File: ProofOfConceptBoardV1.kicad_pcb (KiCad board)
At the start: 2 copper layers, 37 parts, among them U1 MCP2515-EST, U2 MCP2515-EST

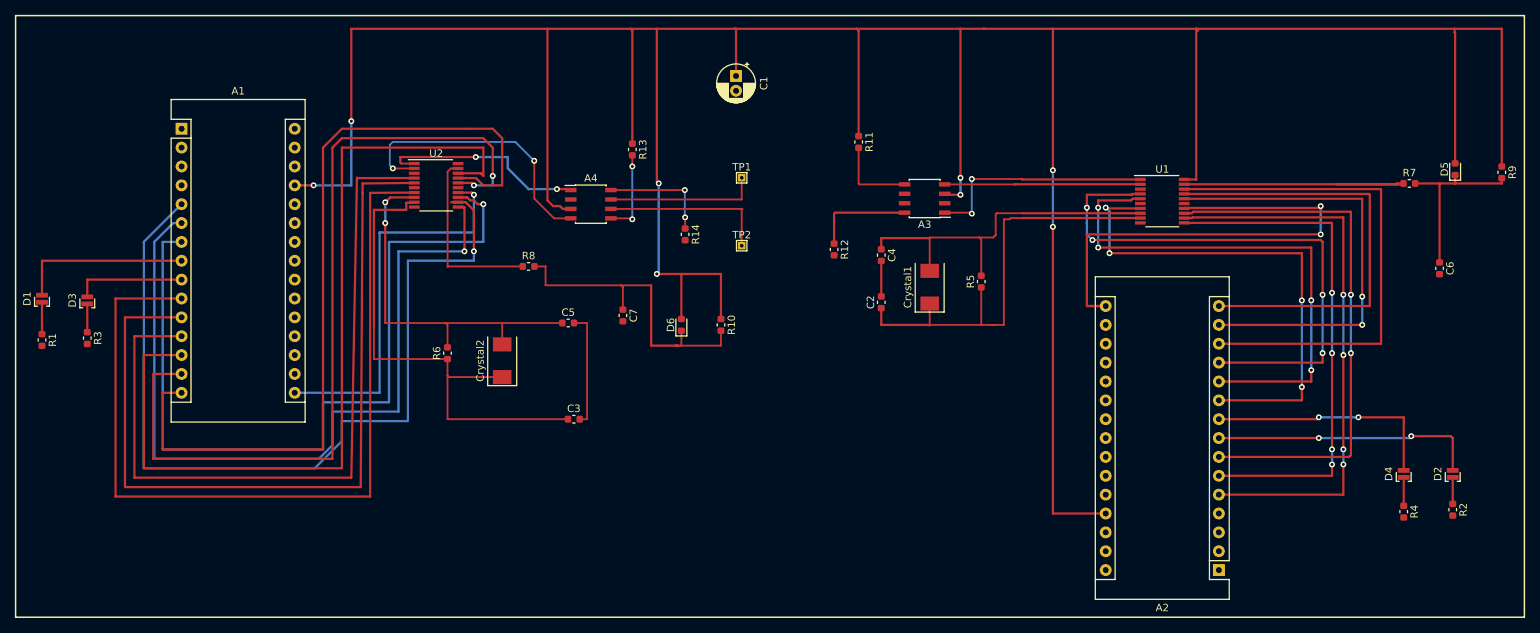
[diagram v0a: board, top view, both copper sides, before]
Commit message: 0.0.4 Fixed some PCB Connections and adjusted Top and Bot Ground Plane
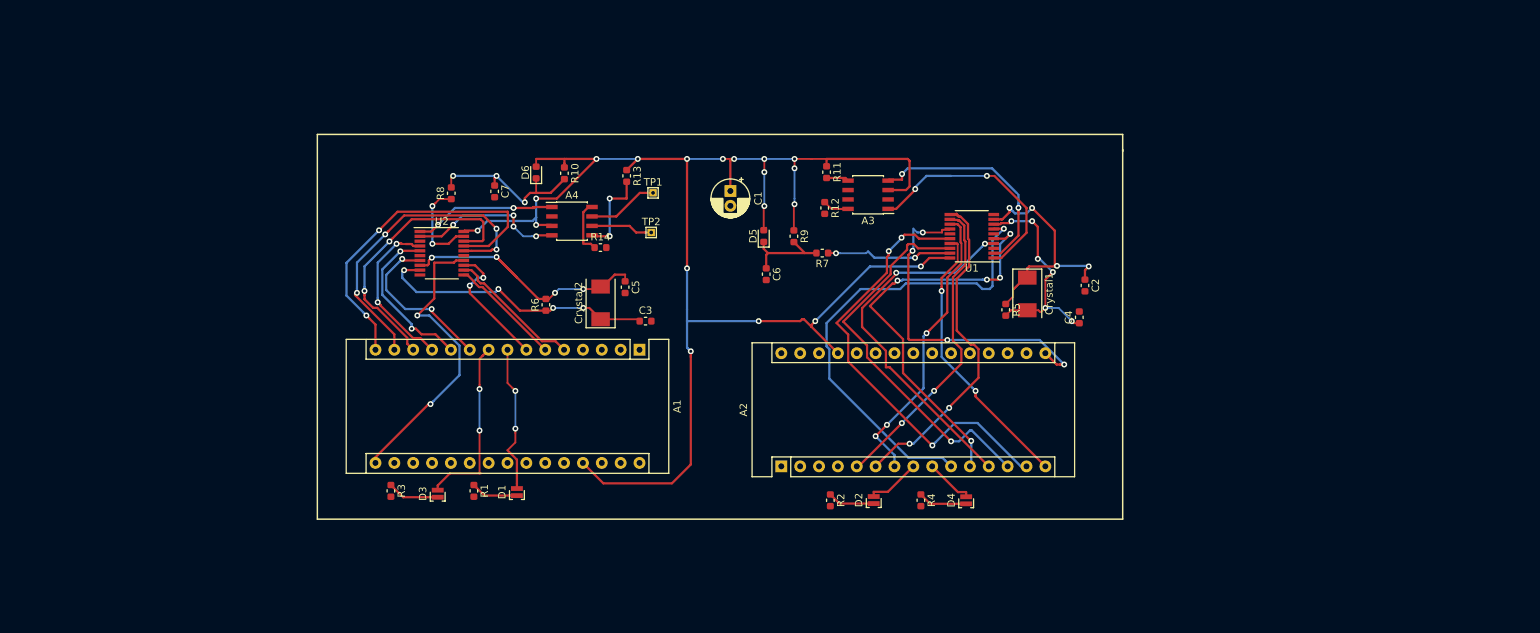
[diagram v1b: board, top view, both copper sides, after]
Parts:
- moved R9 95.7 mm to (133.3, 70.4)
- moved D5 93.6 mm to (129.2, 70.3)
- moved C6 90.7 mm to (129.5, 75.5)
- moved R2 83.8 mm to (138.2, 105.9)
- moved R7 79.6 mm to (137.1, 72.6), turned to 180 degrees
- moved D2 78.1 mm to (144.0, 105.9)
- moved D1 69.1 mm to (96.0, 104.8)
- moved A1 68.5 mm to (112.5, 85.6), turned to 270 degrees
- moved R4 65.0 mm to (150.4, 105.9)
- moved R1 61.6 mm to (90.2, 104.6)
- moved A2 60.6 mm to (131.6, 101.3), turned to 90 degrees
- moved D4 59.0 mm to (156.5, 105.9)
- moved D3 53.9 mm to (85.3, 105.0)
- moved R3 45.8 mm to (79.0, 104.6)
- moved R10 29.4 mm to (102.4, 61.9)
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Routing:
- net +5V: track 457.3 -> 216.8 mm, vias 8 -> 19
- net INT0_2: track 118.2 -> 18.3 mm, vias 1 -> 0
- net TBUF0_2: track 116.7 -> 22.4 mm, vias 0 -> 2
- net INT1_2: track 109.3 -> 15.2 mm, vias 1 -> 0
- net INTMCP_2: track 110.5 -> 17.7 mm, vias 1 -> 2
- net TBUF1_2: track 110.1 -> 22.2 mm, vias 0 -> 2
- net TBUF2_2: track 102.7 -> 22.6 mm, vias 0 -> 2
- net SS_2: track 116.6 -> 38.2 mm, vias 0 -> 2
- net MOSI_2: track 113.8 -> 43.6 mm, vias 2 -> 4
- net MISO_2: track 110.8 -> 46.9 mm, vias 0 -> 2
- net INT0: track 75.6 -> 41.9 mm, vias 4 -> 2
- net INTMCP: track 73.2 -> 39.7 mm, vias 2 -> 3
- net OSC1_2: track 68.1 -> 38.4 mm, vias 0 -> 4
- net Net-(A2-Pad8): track 36.1 -> 7.39 mm, vias 2 -> 0
- net OSC1: track 60.4 -> 34.7 mm, vias 0 -> 4
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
